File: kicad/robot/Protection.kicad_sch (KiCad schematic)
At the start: 23 parts, among them Q2 EFC8811R-TF, U12 BQ27742YZFR-G1

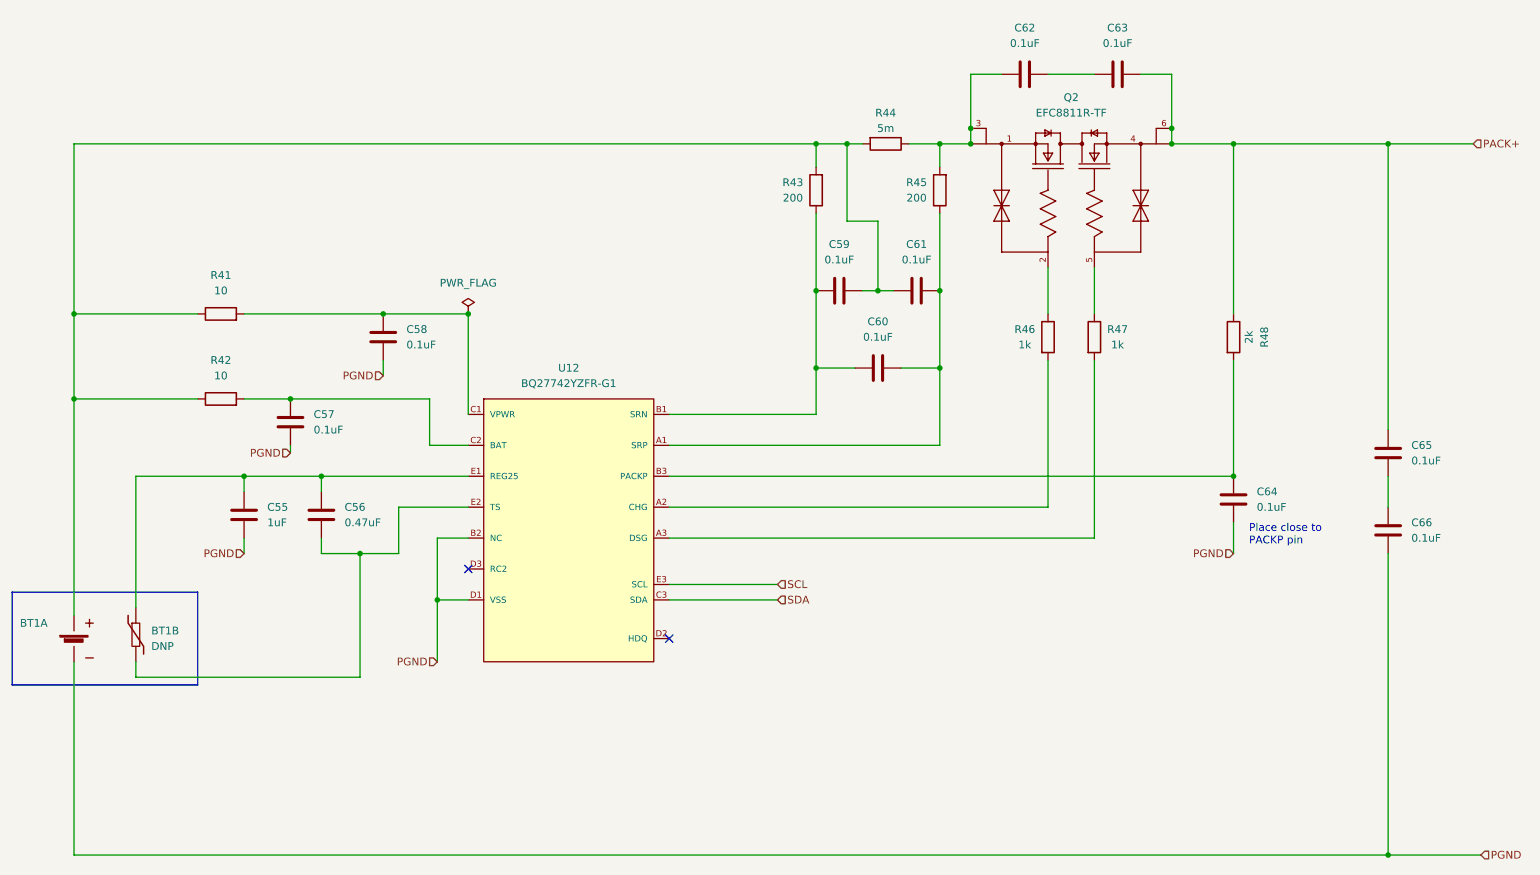
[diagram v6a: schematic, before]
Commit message: Bulk capacitor field edits
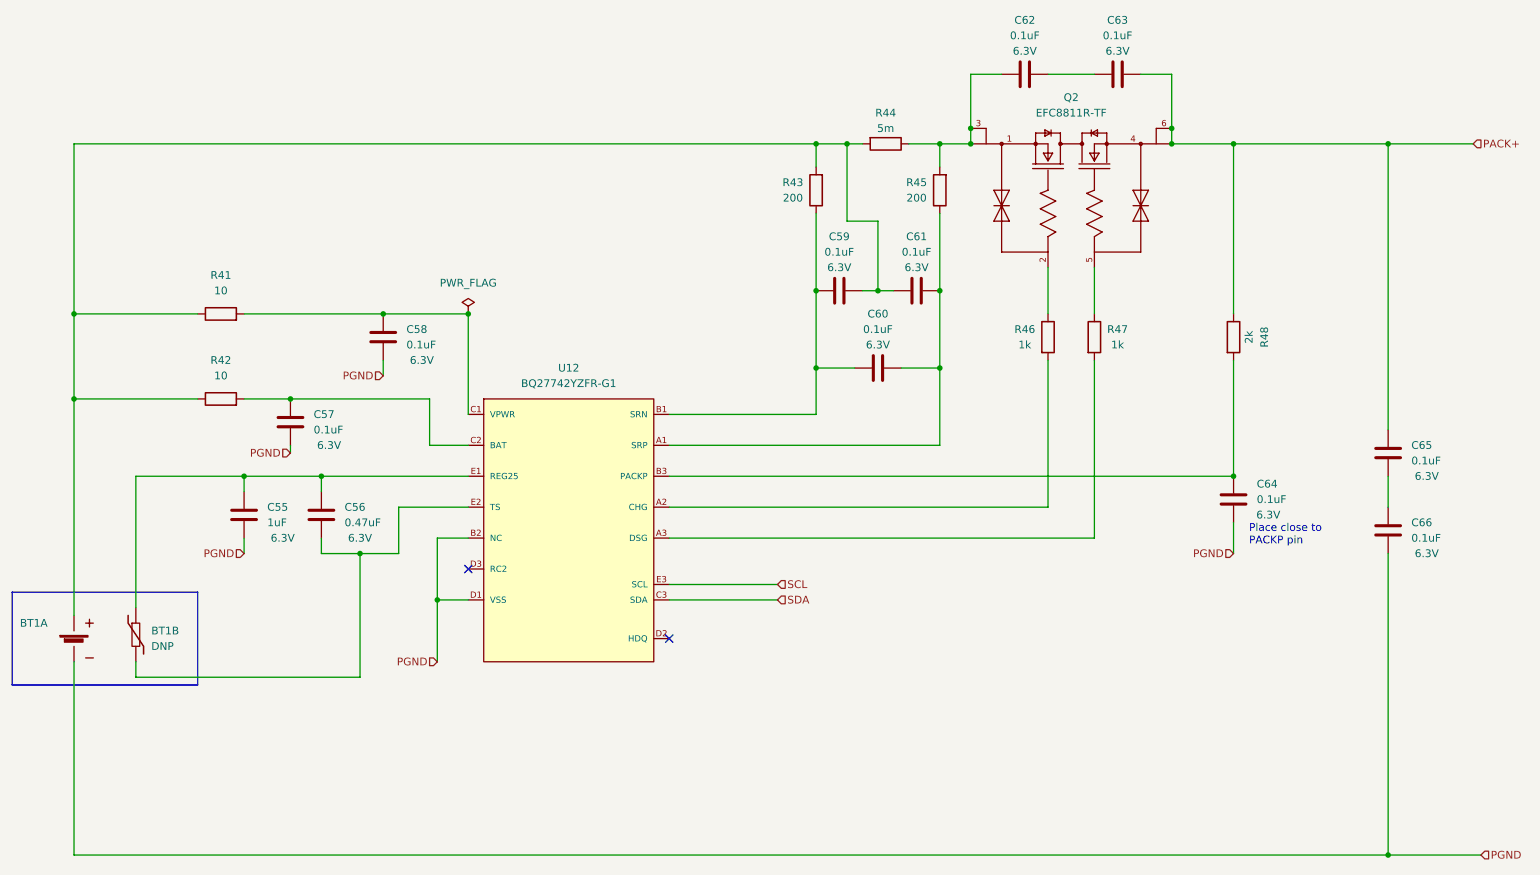
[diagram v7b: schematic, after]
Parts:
- C55: Manufacturer Samsung -> (none); Part Number CL10A105KQ8NNNC -> (none)
- C56: Manufacturer Samsung -> (none); Part Number CL10B474KO8NNNC -> (none)
- C57, C58, C59, C60, C61, C62, C63, C64, C65, C66: Manufacturer Samsung -> (none); Part Number CL10B104KB8NNWC -> (none)
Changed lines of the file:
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@@
   )
   (symbol (lib_id "Device:C") (at 287.02 140.97 0) (unit 1)
-    (in_bom yes) (on_board yes) (fields_autoplaced)
-    (property "Reference" "C64" (id 0) (at 290.83 139.6999 0)
-      (effects (font (size 1.27 1.27)) (justify left))
-    )
-    (property "Value" "0.1uF" (id 1) (at 290.83 142.2399 0)
+    (in_bom yes) (on_board yes)
+    (property "Reference" "C64" (id 0) (at 290.83 138.43 0)
+      (effects (font (size 1.27 1.27)) (justify left))
+    )
+    (property "Value" "0.1uF" (id 1) (at 290.83 140.97 0)
       (effects (font (size 1.27 1.27)) (justify left))
     )
@@
       (effects (font (size 1.27 1.27)) hide)
     )
-    (property "Manufacturer" "Samsung" (id 4) (at 287.02 140.97 0)
-      (effects (font (size 1.27 1.27)) hide)
-    )
-    (property "Part Number" "CL10B104KB8NNWC" (id 5) (at 287.02 140.97 0)
-      (effects (font (size 1.27 1.27)) hide)
-    )
+    (property "Description" "6.3V" (id 4) (at 292.735 143.5101 0))
     (pin "1")
     (pin "2")
   )
   (symbol (lib_id "Device:C") (at 267.97 71.12 90) (unit 1)
-    (in_bom yes) (on_board yes) (fields_autoplaced)
-    (property "Reference" "C63" (id 0) (at 267.97 63.5 90))
-    (property "Value" "0.1uF" (id 1) (at 267.97 66.04 90))
+    (in_bom yes) (on_board yes)
+    (property "Reference" "C63" (id 0) (at 267.97 62.23 90))
+    (property "Value" "0.1uF" (id 1) (at 267.97 64.77 90))
     (property "Footprint" "Capacitor_SMD:C_0603_1608Metric" (id 2) (at 271.78 70.1548 0)
       (effects (font (size 1.27 1.27)) hide)
@@
       (effects (font (size 1.27 1.27)) hide)
     )
-    (property "Manufacturer" "Samsung" (id 4) (at 267.97 71.12 0)
-      (effects (font (size 1.27 1.27)) hide)
-    )
-    (property "Part Number" "CL10B104KB8NNWC" (id 5) (at 267.97 71.12 0)
-      (effects (font (size 1.27 1.27)) hide)
-    )
+    (property "Description" "6.3V" (id 4) (at 267.97 67.31 90))
     (pin "1")
     (pin "2")
@@
   )
   (symbol (lib_id "Device:C") (at 312.42 133.35 0) (unit 1)
-    (in_bom yes) (on_board yes) (fields_autoplaced)
+    (in_bom yes) (on_board yes)
     (property "Reference" "C65" (id 0) (at 316.23 132.0799 0)
       (effects (font (size 1.27 1.27)) (justify left))
@@
       (effects (font (size 1.27 1.27)) hide)
     )
-    (property "Manufacturer" "Samsung" (id 4) (at 312.42 133.35 0)
-      (effects (font (size 1.27 1.27)) hide)
-    )
-    (property "Part Number" "CL10B104KB8NNWC" (id 5) (at 312.42 133.35 0)
-      (effects (font (size 1.27 1.27)) hide)
-    )
+    (property "Description" "6.3V" (id 4) (at 318.77 137.16 0))
     (pin "1")
     (pin "2")
   )
   (symbol (lib_id "Device:C") (at 222.25 106.68 90) (unit 1)
-    (in_bom yes) (on_board yes) (fields_autoplaced)
-    (property "Reference" "C59" (id 0) (at 222.25 99.06 90))
-    (property "Value" "0.1uF" (id 1) (at 222.25 101.6 90))
+    (in_bom yes) (on_board yes)
+    (property "Reference" "C59" (id 0) (at 222.25 97.79 90))
+    (property "Value" "0.1uF" (id 1) (at 222.25 100.33 90))
     (property "Footprint" "Capacitor_SMD:C_0603_1608Metric" (id 2) (at 226.06 105.7148 0)
       (effects (font (size 1.27 1.27)) hide)
@@
       (effects (font (size 1.27 1.27)) hide)
     )
-    (property "Manufacturer" "Samsung" (id 4) (at 222.25 106.68 0)
-      (effects (font (size 1.27 1.27)) hide)
-    )
-    (property "Part Number" "CL10B104KB8NNWC" (id 5) (at 222.25 106.68 0)
-      (effects (font (size 1.27 1.27)) hide)
-    )
+    (property "Description" "6.3V" (id 4) (at 222.25 102.87 90))
     (pin "1")
     (pin "2")
   )
   (symbol (lib_id "Device:C") (at 124.46 143.51 0) (unit 1)
-    (in_bom yes) (on_board yes) (fields_autoplaced)
+    (in_bom yes) (on_board yes)
     (property "Reference" "C55" (id 0) (at 128.27 142.2399 0)
       (effects (font (size 1.27 1.27)) (justify left))
@@
       (effects (font (size 1.27 1.27)) hide)
     )
-    (property "Manufacturer" "Samsung" (id 4) (at 124.46 143.51 0)
-      (effects (font (size 1.27 1.27)) hide)
-    )
-    (property "Part Number" "CL10A105KQ8NNNC" (id 5) (at 124.46 143.51 0)
-      (effects (font (size 1.27 1.27)) hide)
-    )
+    (property "Description" "6.3V" (id 4) (at 130.81 147.32 0))
     (pin "1")
     (pin "2")
@@
   )
   (symbol (lib_id "Device:C") (at 234.95 106.68 90) (unit 1)
-    (in_bom yes) (on_board yes) (fields_autoplaced)
-    (property "Reference" "C61" (id 0) (at 234.95 99.06 90))
-    (property "Value" "0.1uF" (id 1) (at 234.95 101.6 90))
+    (in_bom yes) (on_board yes)
+    (property "Reference" "C61" (id 0) (at 234.95 97.79 90))
+    (property "Value" "0.1uF" (id 1) (at 234.95 100.33 90))
     (property "Footprint" "Capacitor_SMD:C_0603_1608Metric" (id 2) (at 238.76 105.7148 0)
       (effects (font (size 1.27 1.27)) hide)
@@
       (effects (font (size 1.27 1.27)) hide)
     )
-    (property "Manufacturer" "Samsung" (id 4) (at 234.95 106.68 0)
-      (effects (font (size 1.27 1.27)) hide)
-    )
-    (property "Part Number" "CL10B104KB8NNWC" (id 5) (at 234.95 106.68 0)
-      (effects (font (size 1.27 1.27)) hide)
-    )
+    (property "Description" "6.3V" (id 4) (at 234.95 102.87 90))
     (pin "1")
     (pin "2")
   )
   (symbol (lib_id "Device:C") (at 252.73 71.12 90) (unit 1)
-    (in_bom yes) (on_board yes) (fields_autoplaced)
-    (property "Reference" "C62" (id 0) (at 252.73 63.5 90))
-    (property "Value" "0.1uF" (id 1) (at 252.73 66.04 90))
+    (in_bom yes) (on_board yes)
+    (property "Reference" "C62" (id 0) (at 252.73 62.23 90))
+    (property "Value" "0.1uF" (id 1) (at 252.73 64.77 90))
     (property "Footprint" "Capacitor_SMD:C_0603_1608Metric" (id 2) (at 256.54 70.1548 0)
       (effects (font (size 1.27 1.27)) hide)
@@
       (effects (font (size 1.27 1.27)) hide)
     )
-    (property "Manufacturer" "Samsung" (id 4) (at 252.73 71.12 0)
-      (effects (font (size 1.27 1.27)) hide)
-    )
-    (property "Part Number" "CL10B104KB8NNWC" (id 5) (at 252.73 71.12 0)
-      (effects (font (size 1.27 1.27)) hide)
-    )
+    (property "Description" "6.3V" (id 4) (at 252.73 67.31 90))
     (pin "1")
     (pin "2")
   )
   (symbol (lib_id "Device:C") (at 147.32 114.3 0) (unit 1)
-    (in_bom yes) (on_board yes) (fields_autoplaced)
+    (in_bom yes) (on_board yes)
     (property "Reference" "C58" (id 0) (at 151.13 113.0299 0)
       (effects (font (size 1.27 1.27)) (justify left))
@@
       (effects (font (size 1.27 1.27)) hide)
     )
-    (property "Manufacturer" "Samsung" (id 4) (at 147.32 114.3 0)
-      (effects (font (size 1.27 1.27)) hide)
-    )
-    (property "Part Number" "CL10B104KB8NNWC" (id 5) (at 147.32 114.3 0)
-      (effects (font (size 1.27 1.27)) hide)
-    )
+    (property "Description" "6.3V" (id 4) (at 153.67 118.11 0))
     (pin "1")
     (pin "2")
   )
   (symbol (lib_id "Device:C") (at 312.42 146.05 0) (unit 1)
-    (in_bom yes) (on_board yes) (fields_autoplaced)
+    (in_bom yes) (on_board yes)
     (property "Reference" "C66" (id 0) (at 316.23 144.7799 0)
       (effects (font (size 1.27 1.27)) (justify left))
@@
       (effects (font (size 1.27 1.27)) hide)
     )
-    (property "Manufacturer" "Samsung" (id 4) (at 312.42 146.05 0)
-      (effects (font (size 1.27 1.27)) hide)
-    )
-    (property "Part Number" "CL10B104KB8NNWC" (id 5) (at 312.42 146.05 0)
-      (effects (font (size 1.27 1.27)) hide)
-    )
+    (property "Description" "6.3V" (id 4) (at 318.77 149.86 0))
     (pin "1")
     (pin "2")
   )
   (symbol (lib_id "Device:C") (at 132.08 128.27 0) (unit 1)
-    (in_bom yes) (on_board yes) (fields_autoplaced)
+    (in_bom yes) (on_board yes)
     (property "Reference" "C57" (id 0) (at 135.89 126.9999 0)
       (effects (font (size 1.27 1.27)) (justify left))
@@
       (effects (font (size 1.27 1.27)) hide)
     )
-    (property "Manufacturer" "Samsung" (id 4) (at 132.08 128.27 0)
-      (effects (font (size 1.27 1.27)) hide)
-    )
-    (property "Part Number" "CL10B104KB8NNWC" (id 5) (at 132.08 128.27 0)
-      (effects (font (size 1.27 1.27)) hide)
-    )
+    (property "Description" "6.3V" (id 4) (at 138.43 132.08 0))
     (pin "1")
     (pin "2")
@@
   )
   (symbol (lib_id "Device:C") (at 228.6 119.38 90) (unit 1)
-    (in_bom yes) (on_board yes) (fields_autoplaced)
-    (property "Reference" "C60" (id 0) (at 228.6 111.76 90))
-    (property "Value" "0.1uF" (id 1) (at 228.6 114.3 90))
+    (in_bom yes) (on_board yes)
+    (property "Reference" "C60" (id 0) (at 228.6 110.49 90))
+    (property "Value" "0.1uF" (id 1) (at 228.6 113.03 90))
     (property "Footprint" "Capacitor_SMD:C_0603_1608Metric" (id 2) (at 232.41 118.4148 0)
       (effects (font (size 1.27 1.27)) hide)
@@
       (effects (font (size 1.27 1.27)) hide)
     )
-    (property "Manufacturer" "Samsung" (id 4) (at 228.6 119.38 0)
-      (effects (font (size 1.27 1.27)) hide)
-    )
-    (property "Part Number" "CL10B104KB8NNWC" (id 5) (at 228.6 119.38 0)
-      (effects (font (size 1.27 1.27)) hide)
-    )
+    (property "Description" "6.3V" (id 4) (at 228.6 115.57 90))
     (pin "1")
     (pin "2")
@@
   )
   (symbol (lib_id "Device:C") (at 137.16 143.51 0) (unit 1)
-    (in_bom yes) (on_board yes) (fields_autoplaced)
+    (in_bom yes) (on_board yes)
     (property "Reference" "C56" (id 0) (at 140.97 142.2399 0)
       (effects (font (size 1.27 1.27)) (justify left))
@@
       (effects (font (size 1.27 1.27)) hide)
     )
-    (property "Manufacturer" "Samsung" (id 4) (at 137.16 143.51 0)
-      (effects (font (size 1.27 1.27)) hide)
-    )
-    (property "Part Number" "CL10B474KO8NNNC" (id 5) (at 137.16 143.51 0)
-      (effects (font (size 1.27 1.27)) hide)
-    )
-    (pin "1")
-    (pin "2")
+    (property "Description" "6.3V" (id 4) (at 143.51 147.32 0))
+    (pin "1")
+    (pin "2")

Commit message: bulk footprint updates to capacitors
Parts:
- C55, C57, C58, C59, C60, C61, C62, C63, C64, C65, C66: footprint Capacitor_SMD:C_0603_1608Metric -> Capacitor_SMD:C_0402_1005Metric
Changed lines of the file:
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@@
       (effects (font (size 1.27 1.27)) (justify left))
     )
-    (property "Footprint" "Capacitor_SMD:C_0603_1608Metric" (id 2) (at 287.9852 144.78 0)
+    (property "Footprint" "Capacitor_SMD:C_0402_1005Metric" (id 2) (at 287.9852 144.78 0)
       (effects (font (size 1.27 1.27)) hide)
     )
@@
     (property "Reference" "C63" (id 0) (at 267.97 62.23 90))
     (property "Value" "0.1uF" (id 1) (at 267.97 64.77 90))
-    (property "Footprint" "Capacitor_SMD:C_0603_1608Metric" (id 2) (at 271.78 70.1548 0)
+    (property "Footprint" "Capacitor_SMD:C_0402_1005Metric" (id 2) (at 271.78 70.1548 0)
       (effects (font (size 1.27 1.27)) hide)
     )
@@
       (effects (font (size 1.27 1.27)) (justify left))
     )
-    (property "Footprint" "Capacitor_SMD:C_0603_1608Metric" (id 2) (at 313.3852 137.16 0)
+    (property "Footprint" "Capacitor_SMD:C_0402_1005Metric" (id 2) (at 313.3852 137.16 0)
       (effects (font (size 1.27 1.27)) hide)
     )
@@
     (property "Reference" "C59" (id 0) (at 222.25 97.79 90))
     (property "Value" "0.1uF" (id 1) (at 222.25 100.33 90))
-    (property "Footprint" "Capacitor_SMD:C_0603_1608Metric" (id 2) (at 226.06 105.7148 0)
+    (property "Footprint" "Capacitor_SMD:C_0402_1005Metric" (id 2) (at 226.06 105.7148 0)
       (effects (font (size 1.27 1.27)) hide)
     )
@@
       (effects (font (size 1.27 1.27)) (justify left))
     )
-    (property "Footprint" "Capacitor_SMD:C_0603_1608Metric" (id 2) (at 113.9952 144.78 0)
+    (property "Footprint" "Capacitor_SMD:C_0402_1005Metric" (id 2) (at 113.9952 144.78 0)
       (effects (font (size 1.27 1.27)) hide)
     )
@@
     (property "Reference" "C61" (id 0) (at 234.95 97.79 90))
     (property "Value" "0.1uF" (id 1) (at 234.95 100.33 90))
-    (property "Footprint" "Capacitor_SMD:C_0603_1608Metric" (id 2) (at 238.76 105.7148 0)
+    (property "Footprint" "Capacitor_SMD:C_0402_1005Metric" (id 2) (at 238.76 105.7148 0)
       (effects (font (size 1.27 1.27)) hide)
     )
@@
     (property "Reference" "C62" (id 0) (at 252.73 62.23 90))
     (property "Value" "0.1uF" (id 1) (at 252.73 64.77 90))
-    (property "Footprint" "Capacitor_SMD:C_0603_1608Metric" (id 2) (at 256.54 70.1548 0)
+    (property "Footprint" "Capacitor_SMD:C_0402_1005Metric" (id 2) (at 256.54 70.1548 0)
       (effects (font (size 1.27 1.27)) hide)
     )
@@
       (effects (font (size 1.27 1.27)) (justify left))
     )
-    (property "Footprint" "Capacitor_SMD:C_0603_1608Metric" (id 2) (at 148.2852 118.11 0)
+    (property "Footprint" "Capacitor_SMD:C_0402_1005Metric" (id 2) (at 148.2852 118.11 0)
       (effects (font (size 1.27 1.27)) hide)
     )
@@
       (effects (font (size 1.27 1.27)) (justify left))
     )
-    (property "Footprint" "Capacitor_SMD:C_0603_1608Metric" (id 2) (at 313.3852 149.86 0)
+    (property "Footprint" "Capacitor_SMD:C_0402_1005Metric" (id 2) (at 313.3852 149.86 0)
       (effects (font (size 1.27 1.27)) hide)
     )
@@
       (effects (font (size 1.27 1.27)) (justify left))
     )
-    (property "Footprint" "Capacitor_SMD:C_0603_1608Metric" (id 2) (at 133.0452 132.08 0)
+    (property "Footprint" "Capacitor_SMD:C_0402_1005Metric" (id 2) (at 133.0452 132.08 0)
       (effects (font (size 1.27 1.27)) hide)
     )
@@
     (property "Reference" "C60" (id 0) (at 228.6 110.49 90))
     (property "Value" "0.1uF" (id 1) (at 228.6 113.03 90))
-    (property "Footprint" "Capacitor_SMD:C_0603_1608Metric" (id 2) (at 232.41 118.4148 0)
-      (effects (font (size 1.27 1.27)) hide)
-    )
+    (property "Footprint" "Capacitor_SMD:C_0402_1005Metric" (id 2) (at 232.41 118.4148 0)
+      (effects (font (size 1.27 1.27)) hide)
+    )
